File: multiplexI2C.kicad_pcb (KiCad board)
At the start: 2 copper layers, 48.3 x 71.1 mm, 56 parts, among them J1 Screw_Terminal_01x04, J17 Conn_01x04_Pin, J18 PinSocket_1x20_P2.54mm_Vertic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, J19 PinSocket_1x20_P2.54mm_Vertic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, J2 Screw_Terminal_01x04, J20 Screw_Terminal_01x02, J3 Screw_Terminal_01x04, J4 Screw_Terminal_01x04, J5 Screw_Terminal_01x04, J6 Screw_Terminal_01x04, J7 Screw_Terminal_01x04, J8 Screw_Terminal_01x04, J9 header_0.25sqmm_1x04_P4.2mm_D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, SW1 SW_DIP_x03, U1 TCA9548A

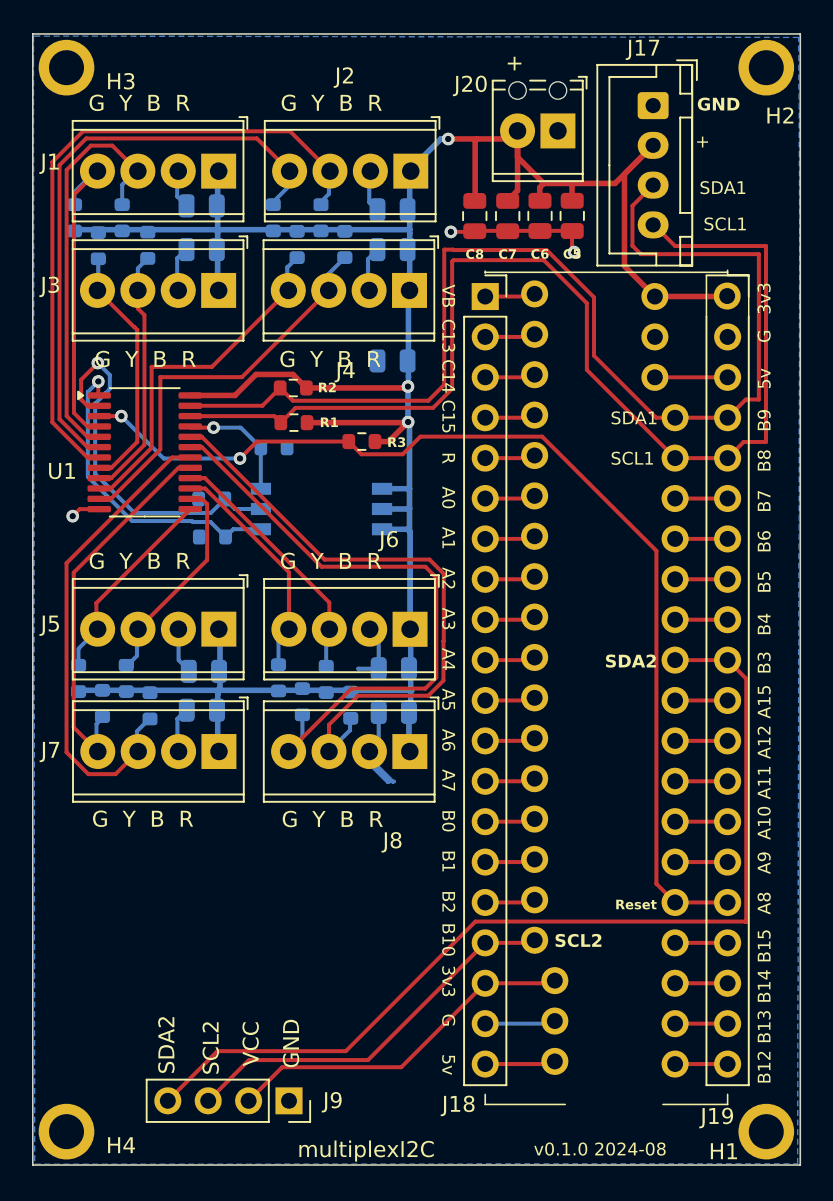
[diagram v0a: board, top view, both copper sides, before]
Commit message: replaced address switch with R0 changeable by solder.
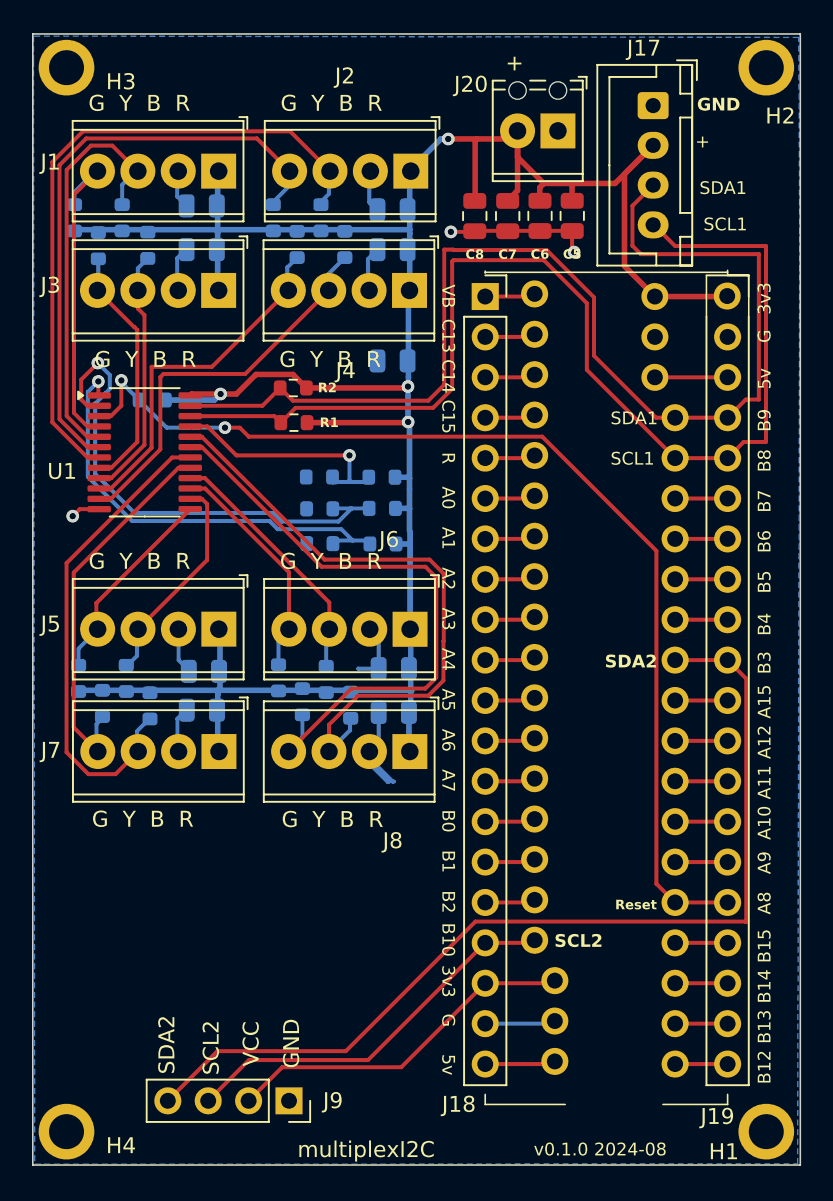
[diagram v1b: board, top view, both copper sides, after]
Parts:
- removed SW1: SW_DIP_x03, ProjectLib:SW_DIP_SPSTx03_Slide_KingTek_DSHP03TS_W7.62mm_P1.27mm
- added R24: 0, ProjectLib:R_0603_1608Metric, B.Cu at (71.5, 52.0)
- added R5: 0, ProjectLib:R_0603_1608Metric, B.Cu at (71.5, 56.2)
- added R6: 0, ProjectLib:R_0603_1608Metric, B.Cu at (71.5, 54.0)
- R23, R25, R4: value 100k -> 0
- R3: moved to B.Cu
- moved R3 13.4 mm to (57.0, 47.1)
- moved R25 7.71 mm to (67.5, 52.0)
- moved R23 6.82 mm to (67.6, 54.0)
- moved R4 6.68 mm to (67.6, 56.2), turned to 180 degrees
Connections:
- R25 pad 1: Net-(U1-A0) -> Net-(U1-A2)
- R4 pad 1: Net-(U1-A2) -> Net-(U1-A0)
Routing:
- net Net-(U1-A0): track 19.8 -> 27.8 mm
- net Net-(U1-A1): track 23.7 -> 31.7 mm
- net Net-(U1-A2): track 7.78 -> 14.8 mm
- net +3V3: track 167.6 -> 165.9 mm, vias 3 -> 4
- net Net-(J19-A8): track 66.1 -> 67.3 mm
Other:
- board text added: "3v3"

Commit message: replaced address switch with R0 changeable by solder. Cleanup.
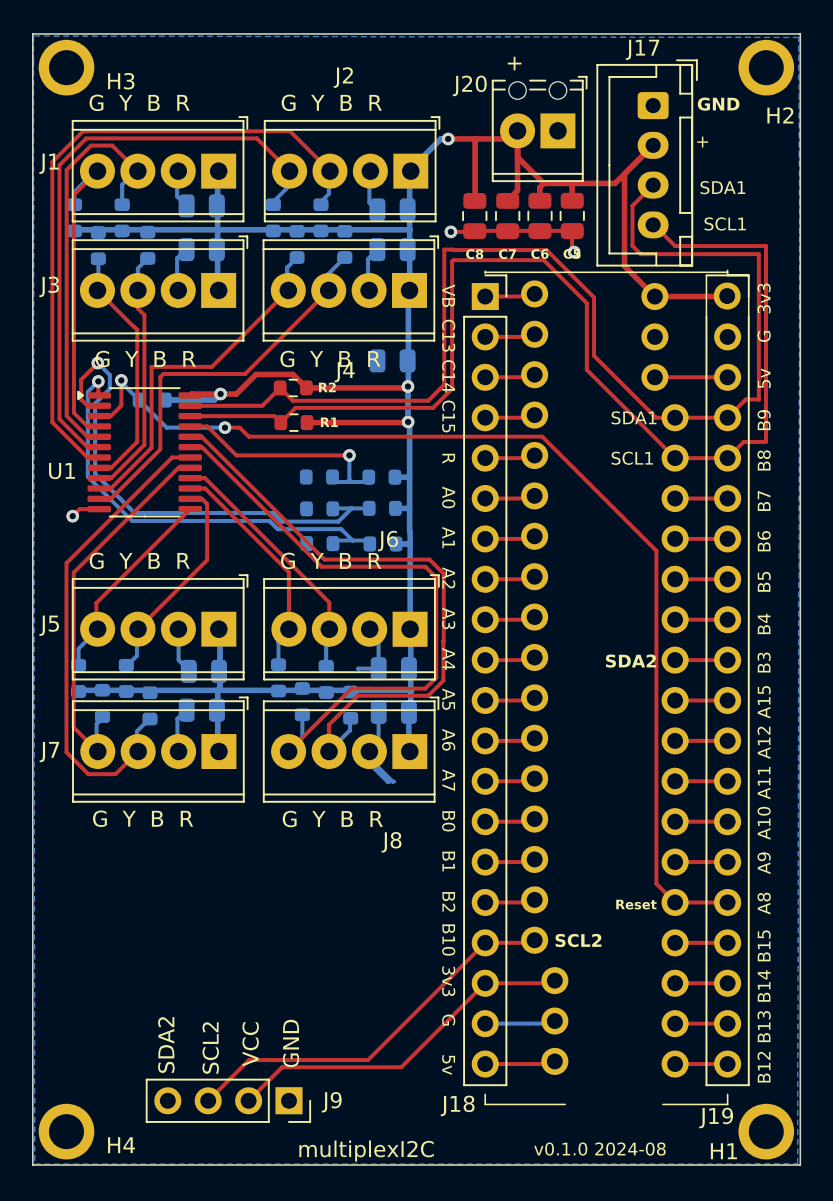
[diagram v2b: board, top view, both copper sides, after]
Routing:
- net /SDA2: track 60.8 -> 2.54 mm
- net GND: track 41.4 -> 40.2 mm
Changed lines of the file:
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@@
 	(segment
 		(start 73.15 40.19)
-		(end 73.15 45.69)
+		(end 73.15 46.44)
 		(width 0.35)
 		(layer "B.Cu")
@@
 	)
 	(segment
-		(start 73.217 52.73)
+		(start 73.217 53.98)
 		(end 73.217 52.06)
-		(width 0.35)
-		(layer "B.Cu")
-		(net 1)
-	)
-	(segment
-		(start 73.15 45.69)
-		(end 73.15 46.44)
 		(width 0.35)
 		(layer "B.Cu")
@@
 	(segment
 		(start 73.23 39.61)
-		(end 73.23 36.69)
+		(end 73.23 36.44)
 		(width 0.35)
 		(layer "B.Cu")
@@
 	)
 	(segment
-		(start 73.217 53.98)
-		(end 73.217 52.73)
-		(width 0.35)
-		(layer "B.Cu")
-		(net 1)
-	)
-	(segment
-		(start 61.15 36.69)
+		(start 61.15 37.69)
 		(end 61.15 32.69)
-		(width 0.35)
-		(layer "B.Cu")
-		(net 1)
-	)
-	(segment
-		(start 73.23 36.69)
-		(end 73.23 36.44)
-		(width 0.35)
-		(layer "B.Cu")
-		(net 1)
-	)
-	(segment
-		(start 61.15 37.69)
-		(end 61.15 36.69)
 		(width 0.35)
 		(layer "B.Cu")
@@
 	)
 	(segment
-		(start 61.16 65.65)
+		(start 61.16 69.15)
 		(end 61.16 65.4)
 		(width 0.35)
@@
 		(start 73.255 55.438)
 		(end 73.255 56.24)
-		(width 0.35)
-		(layer "B.Cu")
-		(net 1)
-	)
-	(segment
-		(start 61.16 69.15)
-		(end 61.16 65.65)
 		(width 0.35)
 		(layer "B.Cu")
@@
 	)
 	(segment
-		(start 70.695 69.25)
-		(end 70.695 69.675)
-		(width 0.25)
-		(layer "B.Cu")
-		(net 2)
-	)
-	(segment
 		(start 58.61 32.69)
 		(end 58.61 34.35)
@@
 	)
 	(segment
-		(start 70.695 69.25)
-		(end 70.695 70.005)
-		(width 0.25)
-		(layer "B.Cu")
-		(net 2)
-	)
-	(segment
 		(start 71.28 64.04)
 		(end 71.28 62.198)
@@
 	)
 	(segment
-		(start 69.21 88.09)
-		(end 61.14 88.09)
-		(width 0.25)
-		(layer "F.Cu")
-		(net 6)
-	)
-	(segment
-		(start 77.36 79.94)
-		(end 69.21 88.09)
-		(width 0.25)
-		(layer "F.Cu")
-		(net 6)
-	)
-	(segment
 		(start 90.678 63.5)
 		(end 93.218 63.5)
-		(width 0.25)
-		(layer "F.Cu")
-		(net 6)
-	)
-	(segment
-		(start 89.96 63.5)
-		(end 90.11 63.65)
-		(width 0.25)
-		(layer "F.Cu")
-		(net 6)
-	)
-	(segment
-		(start 94.356 79.94)
-		(end 77.36 79.94)
-		(width 0.25)
-		(layer "F.Cu")
-		(net 6)
-	)
-	(segment
-		(start 61.14 88.09)
-		(end 58.02 91.21)
-		(width 0.25)
-		(layer "F.Cu")
-		(net 6)
-	)
-	(segment
-		(start 94.393 79.977)
-		(end 94.356 79.94)
-		(width 0.25)
-		(layer "F.Cu")
-		(net 6)
-	)
-	(segment
-		(start 94.393 64.675)
-		(end 94.393 79.977)
-		(width 0.25)
-		(layer "F.Cu")
-		(net 6)
-	)
-	(segment
-		(start 93.218 63.5)
-		(end 94.393 64.675)
 		(width 0.25)
 		(layer "F.Cu")
@@
 	(segment
 		(start 56.215 47.15)
-		(end 56.11 47.15)
-		(width 0.25)
-		(layer "B.Cu")
-		(net 30)
-	)
-	(segment
-		(start 56.215 47.15)
 		(end 57.95 48.885)
 		(width 0.25)
@@
 	)
 	(segment
-		(start 53.65 40.2045)
-		(end 53.597 40.2575)
-		(width 0.25)
-		(layer "B.Cu")
-		(net 42)
-	)
-	(segment
 		(start 54.442499 52.71)
 		(end 57 50.152499)
@@
 	)
 	(segment
-		(start 53.607 61.5575)
-		(end 53.527 61.4775)
-		(width 0.25)
-		(layer "F.Cu")
-		(net 44)
-	)
-	(segment
 		(start 52.41 62.78)
 		(end 52.41 63.9)
@@
 		(layer "B.Cu")
 		(net 47)
-	)
-	(segment
-		(start 53.65 46.805)
-		(end 53.705 46.86)
-		(width 0.25)
-		(layer "F.Cu")
-		(net 48)
 	)
 	(segment
@@
 	)
 	(segment
-		(start 65.12 55.27)
-		(end 64.93 55.27)
-		(width 0.25)
-		(layer "B.Cu")
-		(net 48)
-	)
-	(segment
 		(start 52.99 46.64)
 		(end 52.99 51.97)
@@
 	)
 	(segment
-		(start 65.12 55.27)
+		(start 64.93 55.27)
 		(end 68.93 55.27)
 		(width 0.25)
@@
 	)
 	(segment
-		(start 54.375 46.445)
-		(end 54.1 46.72)
+		(start 53.45 47.37)
+		(end 54.375 46.445)
 		(width 0.25)
 		(layer "B.Cu")
@@
 	)
 	(segment
-		(start 68.425 53.96)
-		(end 68.395 53.99)
-		(width 0.25)
-		(layer "B.Cu")
-		(net 49)
-	)
-	(segment
 		(start 69.54 53.96)
 		(end 68.425 53.96)
@@
 	)
 	(segment
-		(start 54.1 46.72)
-		(end 53.45 47.37)
-		(width 0.25)
-		(layer "B.Cu")
-		(net 49)
-	)
-	(segment
 		(start 65.19 54.79)
 		(end 64.65 54.25)
@@
 		(start 62.333604 50.63)
 		(end 69.44 50.63)
-		(width 0.25)
-		(layer "F.Cu")
-		(net 50)
-	)
-	(segment
-		(start 59.505 48.885)
-		(end 59.43 48.81)
 		(width 0.25)
 		(layer "F.Cu")
@@
 		(net 50)
 	)
-	(segment
-		(start 68.455 52.3)
-		(end 68.425 52.33)
-		(width 0.25)
-		(layer "B.Cu")
-		(net 50)
-	)

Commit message: squeezed connectors closer together to make room for sx127x module.
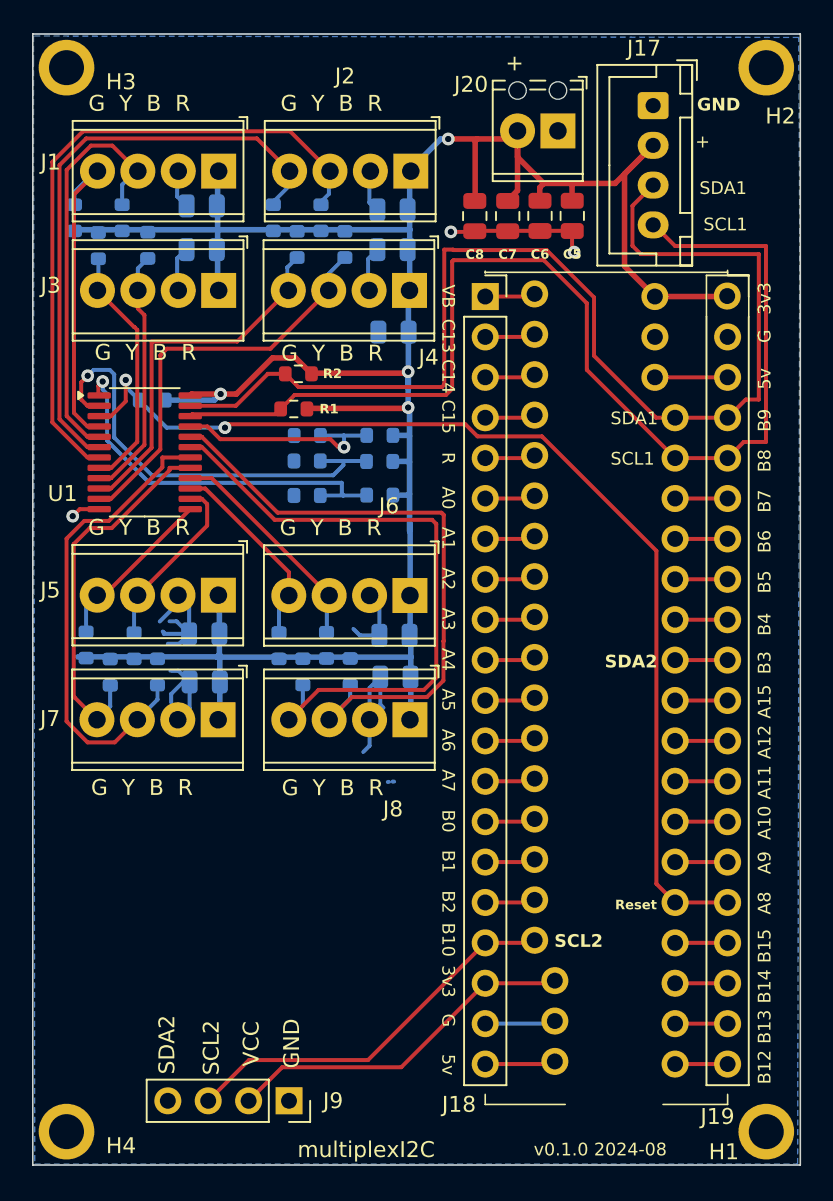
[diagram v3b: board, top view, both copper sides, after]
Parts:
- moved R4 3.13 mm to (66.8, 53.1)
- moved R23 3.11 mm to (66.8, 51.0)
- moved R5 3.08 mm to (71.3, 53.1)
- moved R6 2.95 mm to (71.3, 51.0)
- moved R25 2.72 mm to (66.8, 49.4)
- moved R24 2.63 mm to (71.3, 49.4)
- moved C18 2.36 mm to (60.3, 61.9)
- moved C21 2.22 mm to (72.3, 64.6)
- moved R19 2.18 mm to (57.4, 64.2)
- moved R16 2.15 mm to (52.9, 62.5)
- moved R17 2.14 mm to (68.0, 62.6)
- moved J5 2.14 mm to (61.1, 59.4)
- moved J6 2.12 mm to (73.2, 59.4)
- moved R21 2.12 mm to (69.5, 64.2)
- moved R15 2.11 mm to (55.9, 62.6)
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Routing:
- net GND: track 40.2 -> 52.4 mm
- net Net-(U1-A1): track 31.6 -> 27.7 mm
- net Net-(U1-A0): track 27.7 -> 24.4 mm
- net /Connector5/SD: track 14.4 -> 11.6 mm
- net /Connector4/SC: track 13.4 -> 10.9 mm
- net /Connector4/SD: track 12.6 -> 10.2 mm
- net /Connector5/SC: track 15.6 -> 13.8 mm
- net /Connector7/SD: track 38.9 -> 40.1 mm
- net /Connector3/SD: track 22.3 -> 23.2 mm
- net Net-(U1-A2): track 14.7 -> 13.9 mm
- net /Connector3/SC: track 25.0 -> 25.8 mm

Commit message: added RFM95W pad for sx127x, unpopulated.
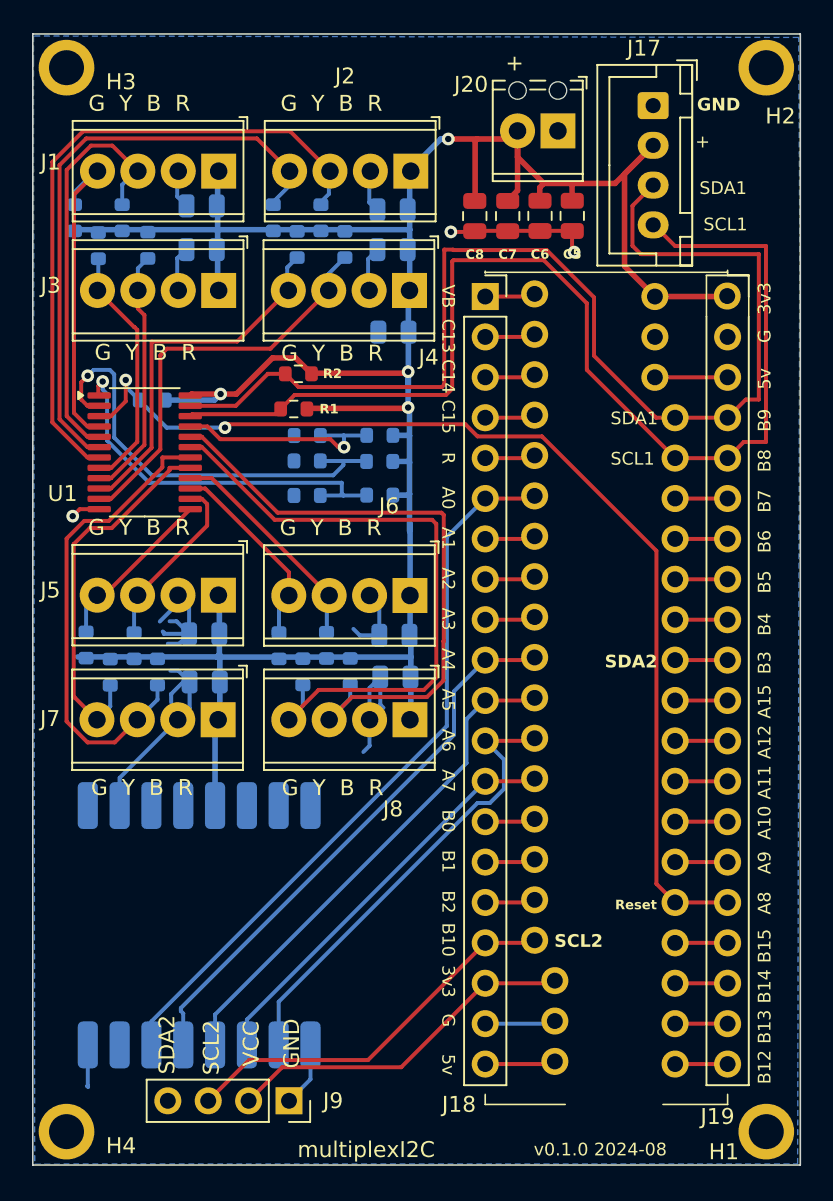
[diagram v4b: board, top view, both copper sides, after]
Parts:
- added U2: RFM95W-915S2, ProjectLib:HOPERF_RFM9XW_SMD, B.Cu at (60.0, 80.2)
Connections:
- net Net-(J18-A0) renamed RESET
- net Net-(J18-A4) renamed NSS
- net Net-(J18-A5) renamed SCK
- net Net-(J18-A6) renamed MISO
- net Net-(J18-A7) renamed MOSI
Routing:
- net RESET: track 3.05 -> 46.1 mm
- net NSS: track 3.05 -> 35.2 mm
- net SCK: track 3.05 -> 31.7 mm
- net MISO: track 3.05 -> 29.0 mm
- net MOSI: track 3.05 -> 25.8 mm
- net GND: track 52.4 -> 66.0 mm
- net +3V3: track 166.4 -> 171.9 mm
